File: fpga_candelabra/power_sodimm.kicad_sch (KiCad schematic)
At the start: 40 parts, among them Q1 AON7544, Q2 AON7544, Q3 AON7544, U18 TPS51716, U19 TLV62130x

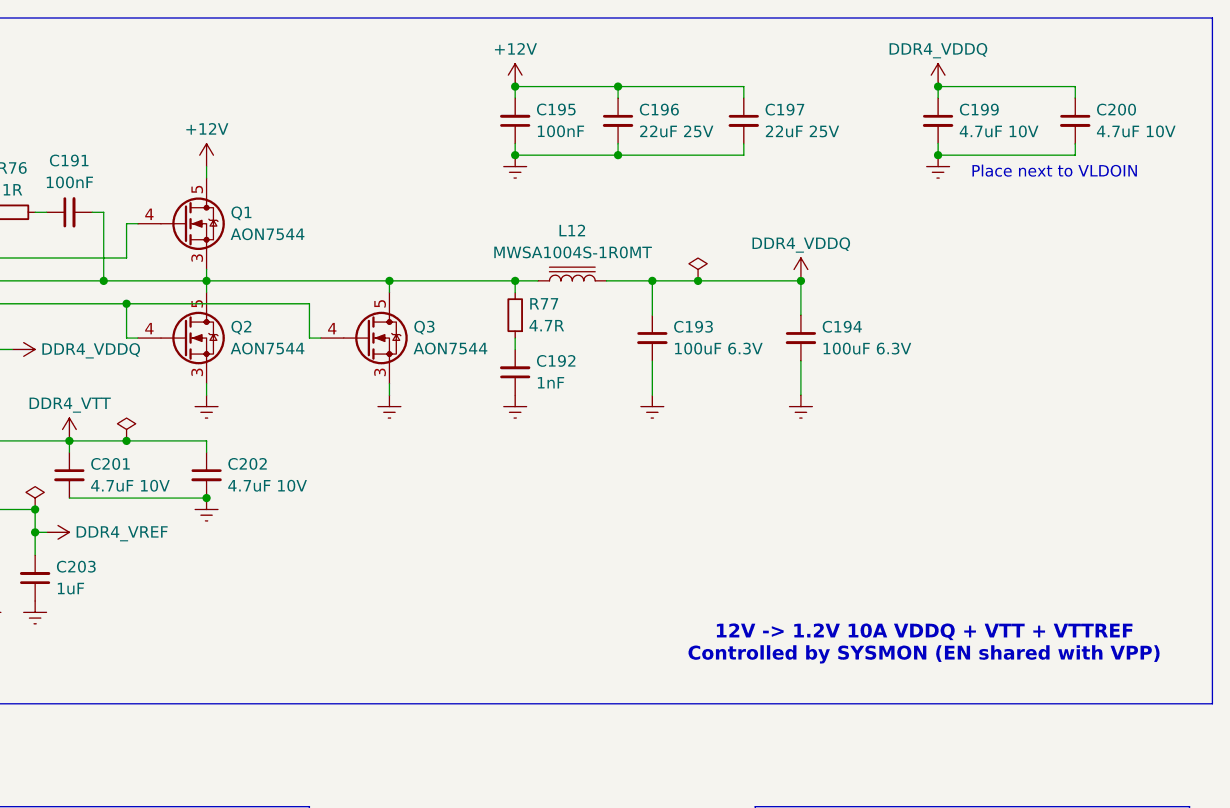
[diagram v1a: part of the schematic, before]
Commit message: fpga_candelabra: major revision
* Finish DDR4 & QSFP+ & PCIe layout
* Change FMC to LPC
* Add mikroBUS extension
* 12V input & PDN updates
* FPGA config updates

Signed-off-by: Yichuan Gao <gaoyichuan000@gmail.com>
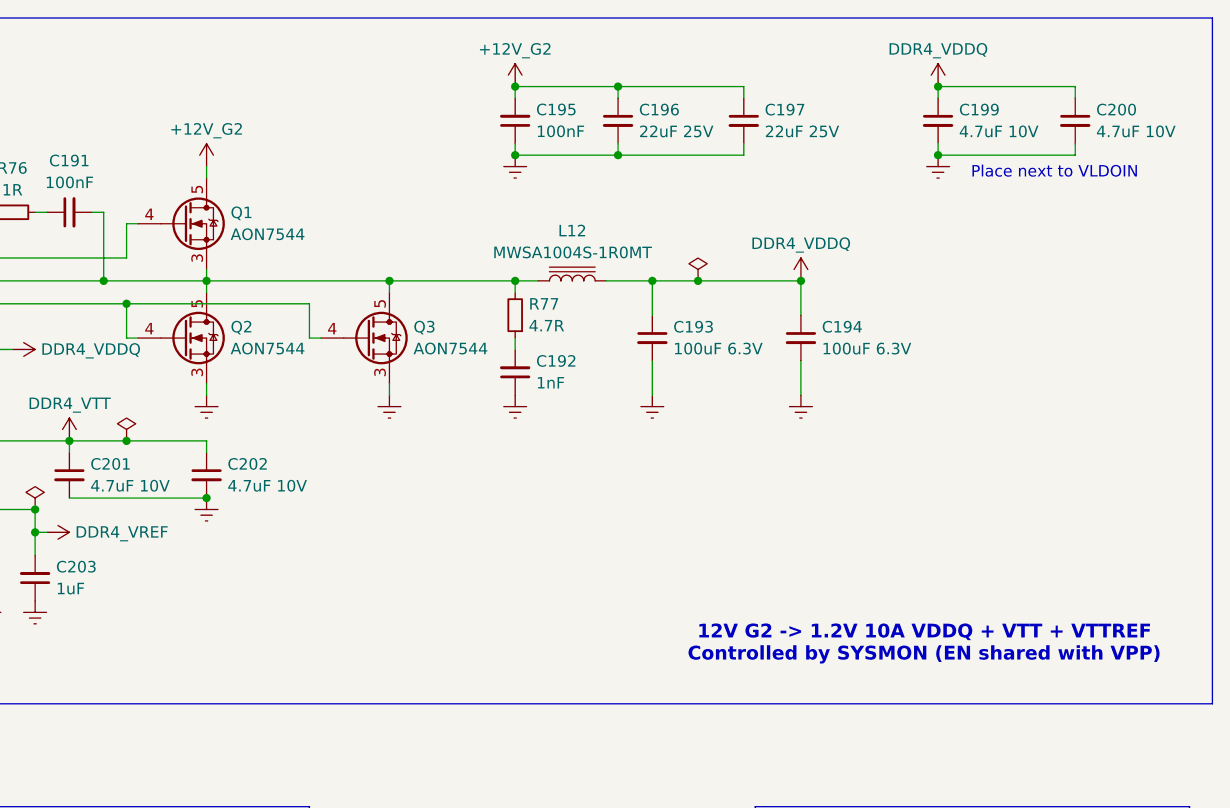
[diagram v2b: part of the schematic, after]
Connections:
- net +12V renamed +12V_G2
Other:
- note added: "12V G2 -> 1.2V 10A VDDQ + VTT + VTTREF Controlled by SYSMON (EN shared with VPP)"
- note removed: "12V -> 1.2V 10A VDDQ + VTT + VTTREF Controlled by SYSMON (EN shared with VPP)"
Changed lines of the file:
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@@
 		)
 	)
-	(text "12V -> 1.2V 10A VDDQ + VTT + VTTREF\nControlled by SYSMON (EN shared with VPP)"
+	(text "12V G2 -> 1.2V 10A VDDQ + VTT + VTTREF\nControlled by SYSMON (EN shared with VPP)"
 		(exclude_from_sim no)
 		(at 209.296 101.346 0)
@@
 			)
 		)
-		(property "Value" "+12V"
+		(property "Value" "+12V_G2"
 			(at 163.83 35.2369 0)
 			(effects
@@
 	)
 	(symbol
-		(lib_id "power:+12V")
-		(at 129.54 48.26 0)
-		(unit 1)
-		(exclude_from_sim no)
-		(in_bom yes)
-		(on_board yes)
-		(dnp no)
-		(fields_autoplaced yes)
-		(property "Reference" "#PWR0222"
-			(at 129.54 52.07 0)
-			(effects
-				(font
-					(size 1.27 1.27)
-				)
-				(hide yes)
-			)
-		)
-		(property "Value" "+12V"
-			(at 129.54 44.1269 0)
-			(effects
-				(font
-					(size 1.27 1.27)
-				)
-			)
-		)
-		(property "Footprint" ""
-			(at 129.54 48.26 0)
-			(effects
-				(font
-					(size 1.27 1.27)
-				)
-				(hide yes)
-			)
-		)
-		(property "Datasheet" ""
-			(at 129.54 48.26 0)
-			(effects
-				(font
-					(size 1.27 1.27)
-				)
-				(hide yes)
-			)
-		)
-		(property "Description" "Power symbol creates a global label with name \"+12V\""
-			(at 129.54 48.26 0)
-			(effects
-				(font
-					(size 1.27 1.27)
-				)
-				(hide yes)
-			)
-		)
-		(pin "1"
-		)
-		(instances
-			(project "fpga_candelabra"
-				(path "/01ed9e92-4e50-4b41-90dc-10444aaec5f7/095efde8-9348-4a17-b275-a6dd2c6e4f2b"
-					(reference "#PWR0222")
-					(unit 1)
-				)
-			)
-		)
-	)
-	(symbol
 		(lib_id "Device:R_Small")
 		(at 114.3 156.21 0)
@@
 					(unit 1)
 				)
+			)
+		)
+	)
+	(symbol
+		(lib_id "power:+12V")
+		(at 129.54 48.26 0)
+		(unit 1)
+		(exclude_from_sim no)
+		(in_bom yes)
+		(on_board yes)
+		(dnp no)
+		(fields_autoplaced yes)
+		(property "Reference" "#PWR0222"
+			(at 129.54 52.07 0)
+			(effects
+				(font
+					(size 1.27 1.27)
+				)
+				(hide yes)
+			)
+		)
+		(property "Value" "+12V_G2"
+			(at 129.54 44.1269 0)
+			(effects
+				(font
+					(size 1.27 1.27)
+				)
+			)
+		)
+		(property "Footprint" ""
+			(at 129.54 48.26 0)
+			(effects
+				(font
+					(size 1.27 1.27)
+				)
+				(hide yes)
+			)
+		)
+		(property "Datasheet" ""
+			(at 129.54 48.26 0)
+			(effects
+				(font
+					(size 1.27 1.27)
+				)
+				(hide yes)
+			)
+		)
+		(property "Description" "Power symbol creates a global label with name \"+12V\""
+			(at 129.54 48.26 0)
+			(effects
+				(font
+					(size 1.27 1.27)
+				)
+				(hide yes)
+			)
+		)
+		(pin "1"
+		)
+		(instances
+			(project "fpga_candelabra"
+				(path "/01ed9e92-4e50-4b41-90dc-10444aaec5f7/095efde8-9348-4a17-b275-a6dd2c6e4f2b"
+					(reference "#PWR0222")
+					(unit 1)
+				)

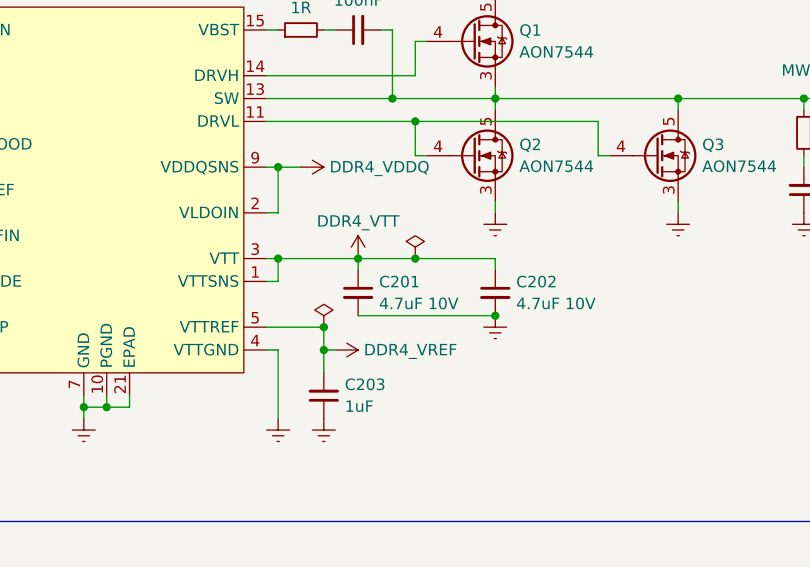
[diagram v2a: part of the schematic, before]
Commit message: fpga_candelabra: sch & layout v0.5, pass basic ERC & DRC
Signed-off-by: Yichuan Gao <gaoyichuan000@gmail.com>
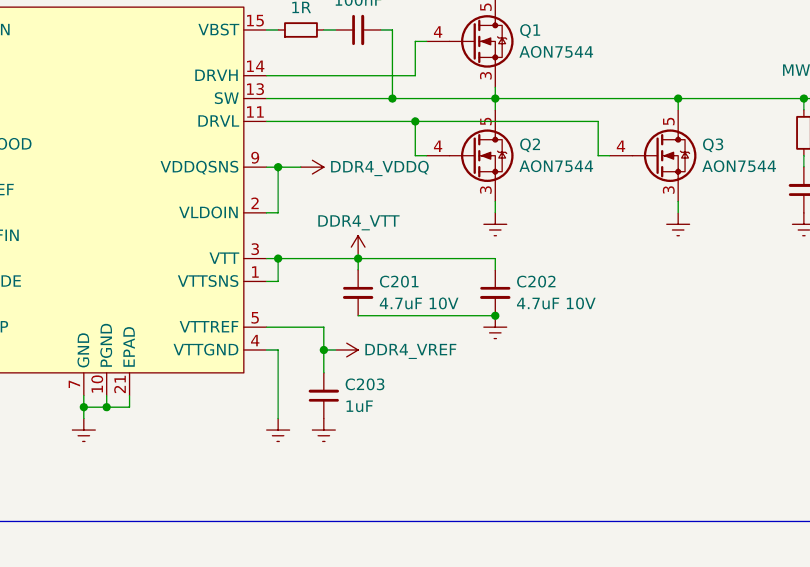
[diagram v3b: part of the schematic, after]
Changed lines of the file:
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@@
 	)
 	(junction
-		(at 120.65 78.74)
-		(diameter 0)
-		(color 0 0 0 0)
-	)
-	(junction
 		(at 82.55 170.18)
 		(diameter 0)
@@
 	)
 	(junction
-		(at 110.49 86.36)
-		(diameter 0)
-		(color 0 0 0 0)
-	)
-	(junction
 		(at 121.92 146.05)
 		(diameter 0)
@@
 	(wire
 		(pts
-			(xy 120.65 78.74) (xy 114.3 78.74)
+			(xy 114.3 78.74) (xy 129.54 78.74)
 		)
 		(stroke
@@
 	(wire
 		(pts
-			(xy 129.54 78.74) (xy 120.65 78.74)
-		)
-		(stroke
-			(width 0)
-			(type default)
-		)
-	)
-	(wire
-		(pts
 			(xy 105.41 96.52) (xy 105.41 88.9)
 		)
@@
 	)
 	(symbol
-		(lib_id "CHIPSAlliance_Power:PWR_FLAG")
-		(at 110.49 86.36 0)
-		(unit 1)
-		(exclude_from_sim no)
-		(in_bom yes)
-		(on_board yes)
-		(dnp no)
-		(fields_autoplaced yes)
-		(property "Reference" "#FLG014"
-			(at 110.49 84.455 0)
-			(effects
-				(font
-					(size 1.27 1.27)
-				)
-				(hide yes)
-			)
-		)
-		(property "Value" "PWR_FLAG"
-			(at 110.49 82.2269 0)
-			(effects
-				(font
-					(size 1.27 1.27)
-				)
-				(hide yes)
-			)
-		)
-		(property "Footprint" ""
-			(at 110.49 86.36 0)
-			(effects
-				(font
-					(size 1.27 1.27)
-				)
-				(hide yes)
-			)
-		)
-		(property "Datasheet" "~"
-			(at 110.49 86.36 0)
-			(effects
-				(font
-					(size 1.27 1.27)
-				)
-				(hide yes)
-			)
-		)
-		(property "Description" "Special symbol for telling ERC where power comes from"
-			(at 110.49 86.36 0)
-			(effects
-				(font
-					(size 1.27 1.27)
-				)
-				(hide yes)
-			)
-		)
-		(pin "1"
-		)
-		(instances
-			(project "fpga_candelabra"
-				(path "/01ed9e92-4e50-4b41-90dc-10444aaec5f7/095efde8-9348-4a17-b275-a6dd2c6e4f2b"
-					(reference "#FLG014")
-					(unit 1)
-				)
-			)
-		)
-	)
-	(symbol
 		(lib_id "Device:L_Iron")
 		(at 104.14 146.05 90)
@@
 					(unit 1)
 				)
-			)
-		)
-	)
-	(symbol
-		(lib_id "CHIPSAlliance_Power:PWR_FLAG")
-		(at 120.65 78.74 0)
-		(unit 1)
-		(exclude_from_sim no)
-		(in_bom yes)
-		(on_board yes)
-		(dnp no)
-		(fields_autoplaced yes)
-		(property "Reference" "#FLG013"
-			(at 120.65 76.835 0)
-			(effects
-				(font
-					(size 1.27 1.27)
-				)
-				(hide yes)
-			)
-		)
-		(property "Value" "PWR_FLAG"
-			(at 120.65 74.6069 0)
-			(effects
-				(font
-					(size 1.27 1.27)
-				)
-				(hide yes)
-			)
-		)
-		(property "Footprint" ""
-			(at 120.65 78.74 0)
-			(effects
-				(font
-					(size 1.27 1.27)
-				)
-				(hide yes)
-			)
-		)
-		(property "Datasheet" "~"
-			(at 120.65 78.74 0)
-			(effects
-				(font
-					(size 1.27 1.27)
-				)
-				(hide yes)
-			)
-		)
-		(property "Description" "Special symbol for telling ERC where power comes from"
-			(at 120.65 78.74 0)
-			(effects
-				(font
-					(size 1.27 1.27)
-				)
-				(hide yes)
-			)
-		)
-		(pin "1"
-		)
-		(instances
-			(project "fpga_candelabra"
-				(path "/01ed9e92-4e50-4b41-90dc-10444aaec5f7/095efde8-9348-4a17-b275-a6dd2c6e4f2b"
-					(reference "#FLG013")
-					(unit 1)
-				)

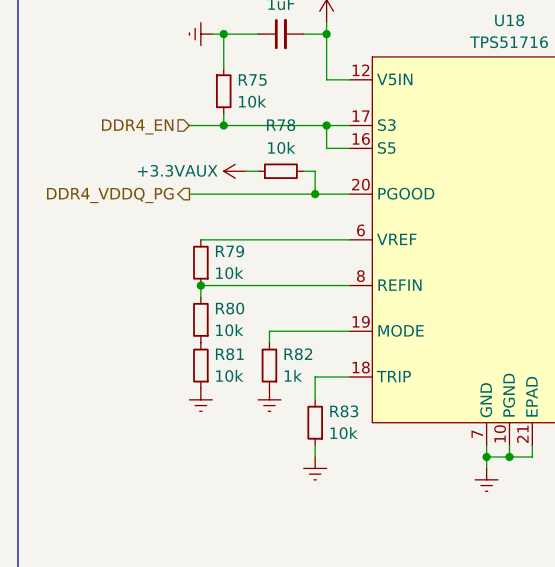
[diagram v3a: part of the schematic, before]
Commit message: fpga_candelabra: first rev fixes - fix vccint power stage FCCM mode - add ddr4 vref decoupling cap - refactor status LEDs - minor layout changes
Signed-off-by: Yichuan Gao <gaoyichuan000@gmail.com>
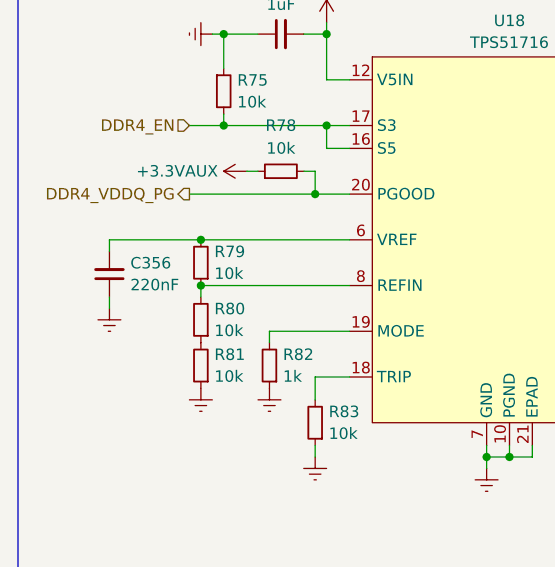
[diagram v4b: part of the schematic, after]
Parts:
- added C356: 220nF, Capacitor_SMD:C_0402_1005Metric, symbol Device:C_Small
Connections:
- net Earth: now also C356.1
- net at R79.2, U18.6 (VREF): now also C356.2
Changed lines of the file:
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@@
 	)
 	(junction
+		(at 52.07 71.12)
+		(diameter 0)
+		(color 0 0 0 0)
+	)
+	(junction
 		(at 121.92 146.05)
 		(diameter 0)
@@
 	(wire
 		(pts
+			(xy 41.91 72.39) (xy 41.91 71.12)
+		)
+		(stroke
+			(width 0)
+			(type default)
+		)
+	)
+	(wire
+		(pts
 			(xy 87.63 170.18) (xy 82.55 170.18)
 		)
@@
 	(wire
 		(pts
+			(xy 41.91 77.47) (xy 41.91 78.74)
+		)
+		(stroke
+			(width 0)
+			(type default)
+		)
+	)
+	(wire
+		(pts
 			(xy 73.66 133.35) (xy 83.82 133.35)
 		)
@@
 	(wire
 		(pts
+			(xy 41.91 71.12) (xy 52.07 71.12)
+		)
+		(stroke
+			(width 0)
+			(type default)
+		)
+	)
+	(wire
+		(pts
 			(xy 121.92 146.05) (xy 114.3 146.05)
 		)
@@
 	)
 	(symbol
+		(lib_id "power:Earth")
+		(at 41.91 78.74 0)
+		(unit 1)
+		(exclude_from_sim no)
+		(in_bom yes)
+		(on_board yes)
+		(dnp no)
+		(fields_autoplaced yes)
+		(property "Reference" "#PWR0486"
+			(at 41.91 85.09 0)
+			(effects
+				(font
+					(size 1.27 1.27)
+				)
+				(hide yes)
+			)
+		)
+		(property "Value" "Earth"
+			(at 41.91 82.8731 0)
+			(effects
+				(font
+					(size 1.27 1.27)
+				)
+				(hide yes)
+			)
+		)
+		(property "Footprint" ""
+			(at 41.91 78.74 0)
+			(effects
+				(font
+					(size 1.27 1.27)
+				)
+				(hide yes)
+			)
+		)
+		(property "Datasheet" "~"
+			(at 41.91 78.74 0)
+			(effects
+				(font
+					(size 1.27 1.27)
+				)
+				(hide yes)
+			)
+		)
+		(property "Description" "Power symbol creates a global label with name \"Earth\""
+			(at 41.91 78.74 0)
+			(effects
+				(font
+					(size 1.27 1.27)
+				)
+				(hide yes)
+			)
+		)
+		(pin "1"
+		)
+		(instances
+			(project "fpga_candelabra"
+				(path "/01ed9e92-4e50-4b41-90dc-10444aaec5f7/095efde8-9348-4a17-b275-a6dd2c6e4f2b"
+					(reference "#PWR0486")
+					(unit 1)
+				)
+			)
+		)
+	)
+	(symbol
 		(lib_id "Device:C_Small")
 		(at 195.58 67.31 0)
@@
 					(unit 1)
 				)
+			)
+		)
+	)
+	(symbol
+		(lib_id "Device:C_Small")
+		(at 41.91 74.93 180)
+		(unit 1)
+		(exclude_from_sim no)
+		(in_bom yes)
+		(on_board yes)
+		(dnp no)
+		(fields_autoplaced yes)
+		(property "Reference" "C356"
+			(at 44.2341 73.7114 0)
+			(effects
+				(font
+					(size 1.27 1.27)
+				)
+				(justify right)
+			)
+		)
+		(property "Value" "220nF"
+			(at 44.2341 76.1357 0)
+			(effects
+				(font
+					(size 1.27 1.27)
+				)
+				(justify right)
+			)
+		)
+		(property "Footprint" "Capacitor_SMD:C_0402_1005Metric"
+			(at 41.91 74.93 0)
+			(effects
+				(font
+					(size 1.27 1.27)
+				)
+				(hide yes)
+			)
+		)
+		(property "Datasheet" "~"
+			(at 41.91 74.93 0)
+			(effects
+				(font
+					(size 1.27 1.27)
+				)
+				(hide yes)
+			)
+		)
+		(property "Description" "Unpolarized capacitor, small symbol"
+			(at 41.91 74.93 0)
+			(effects
+				(font
+					(size 1.27 1.27)
+				)
+				(hide yes)
+			)
+		)
+		(pin "1"
+		)
+		(pin "2"
+		)
+		(instances
+			(project "fpga_candelabra"
+				(path "/01ed9e92-4e50-4b41-90dc-10444aaec5f7/095efde8-9348-4a17-b275-a6dd2c6e4f2b"
+					(reference "C356")
+					(unit 1)
+				)

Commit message: fpga_candelabra: add author & rev to schematics
Signed-off-by: Yichuan Gao <gaoyichuan000@gmail.com>
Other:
- company: (none) -> CHIPS Alliance
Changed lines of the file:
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@@
 	(title_block
 		(title "Power DDR4 SODIMM")
+		(date "2025-02-05")
+		(rev "0.2.0")
+		(company "CHIPS Alliance")
+		(comment 1 "Yichuan Gao")
+		(comment 2 "Yichuan Gao")
 	)
 	(junction

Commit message: fpga_candelabra: update to kicad 9.0
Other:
- company: CHIPS Alliance -> Sipeed

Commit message: fpga_candelabra: update to kicad 10 and fix some 3d model path
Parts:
- U18: footprint Package_DFN_QFN:WQFN-20-1EP_3x3mm_P0.4mm_EP1.7x1.7mm -> CHIPSAlliance_Package_DFN_QFN:WQFN-20-1EP_3x3mm_P0.4mm_EP1.7x1.7mm
